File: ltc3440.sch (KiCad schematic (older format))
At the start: 13 parts, among them U1 LTC3440EDD

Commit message: fix 1.5 mhz rt val
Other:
- note added: "RT=60.4k, fsw=1MHz\nRT=45.3k, fsw=1.5MHz\n"
- note removed: "RT=60.4k, fsw=1MHz\nRT=40.4k, fsw=1.5MHz\n"
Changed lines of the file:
@@
 Fixed Freq. Mode
 Text Notes 4400 4950 0    50   ~ 0
-RT=60.4k, fsw=1MHz\nRT=40.4k, fsw=1.5MHz\n
+RT=60.4k, fsw=1MHz\nRT=45.3k, fsw=1.5MHz\n
 $Comp
 L Device:R_Small RT1

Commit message: adds L1 val
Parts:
- L1: value L_Small -> 4.7uH
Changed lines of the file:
@@
 $EndDescr
-$Comp
-L ltc3440:LTC3440EDD U1
-U 1 1 5F6AED89
-P 5600 3600
-F 0 "U1" H 5150 4050 50  0000 C CNN
-F 1 "LTC3440EDD" H 6000 3050 50  0000 C CNN
-F 2 "Package_DFN_QFN:DFN-10-1EP_3x3mm_P0.5mm_EP1.65x2.38mm" H 5750 3050 50  0001 L CNN
-F 3 "https://www.analog.com/media/en/technical-documentation/data-sheets/3440fd.pdf" H 5600 3550 50  0001 C CNN
-F 4 "LTC3440EDD#TRPBFCT-ND" H 5600 3600 50  0001 C CNN "Digikey_PN"
-F 5 "LTC3440EDD#TRPBF" H 5600 3600 50  0001 C CNN "MPN"
-	1    5600 3600
-	1    0    0    -1
-$EndComp
-$Comp
-L Device:L_Small L1
-U 1 1 5F6B38BC
-P 5600 2950
-F 0 "L1" V 5785 2950 50  0000 C CNN
-F 1 "L_Small" V 5694 2950 50  0000 C CNN
-F 2 "" H 5600 2950 50  0001 C CNN
-F 3 "~" H 5600 2950 50  0001 C CNN
-F 4 "CDR43-4R7M" V 5600 2950 50  0001 C CNN "MPN"
-F 5 "SUMIDA " V 5600 2950 50  0001 C CNN "Manufacturer"
-	1    5600 2950
-	0    -1   -1   0
-$EndComp
 $Comp
 L Device:R_Small R1
@@
 $EndComp
 $Comp
-L Device:R_Small R5
-U 1 1 5F6BE50F
-P 7050 3400
-F 0 "R5" H 7109 3446 50  0000 L CNN
-F 1 "10k" H 7109 3355 50  0000 L CNN
-F 2 "" H 7050 3400 50  0001 C CNN
-F 3 "~" H 7050 3400 50  0001 C CNN
-	1    7050 3400
-	1    0    0    -1
-$EndComp
-$Comp
 L power:+3.3V #PWR03
 U 1 1 5F6C1CB3
@@
 Connection ~ 4450 2950
 Wire Wire Line
-	6100 3700 6150 3700
-Wire Wire Line
 	6400 3700 6500 3700
 Wire Wire Line
 	6700 3700 6800 3700
-Wire Wire Line
-	6800 3700 6800 3950
 Wire Wire Line
 	6800 3700 6800 3600
 Connection ~ 6800 3700
 Wire Wire Line
-	6150 3700 6150 3950
-Wire Wire Line
-	6150 3950 6350 3950
-Connection ~ 6150 3700
-Wire Wire Line
-	6150 3700 6200 3700
-Wire Wire Line
-	6550 3950 6800 3950
-Connection ~ 6800 3950
-Wire Wire Line
-	6800 3950 6800 4000
-Wire Wire Line
 	6800 4200 6800 4300
 Wire Wire Line
 	6800 4300 5700 4300
 Connection ~ 5700 4300
-Wire Wire Line
-	7050 3500 7050 3600
-Wire Wire Line
-	7050 3600 6800 3600
 Connection ~ 6800 3600
 Wire Wire Line
 	6800 3600 6800 3500
 Wire Wire Line
-	7050 3600 7350 3600
-Wire Wire Line
 	7350 3600 7350 3700
-Connection ~ 7050 3600
 Wire Wire Line
 	7350 3900 7350 4300
@@
 Connection ~ 6800 4300
 Wire Wire Line
-	7050 3250 7050 3300
-Wire Wire Line
 	7050 2800 7050 3000
 Wire Wire Line
@@
 Connection ~ 7050 3000
 Wire Wire Line
-	7050 3000 7050 3050
-Wire Wire Line
 	7050 3000 7350 3000
 Wire Wire Line
 	7350 3000 7350 3600
 Connection ~ 7350 3600
-$Comp
-L Device:C_Small C5
-U 1 1 5F6BD824
-P 6450 3950
-F 0 "C5" V 6350 4050 50  0000 C CNN
-F 1 "10pF" V 6350 3850 50  0000 C CNN
-F 2 "" H 6450 3950 50  0001 C CNN
-F 3 "~" H 6450 3950 50  0001 C CNN
-	1    6450 3950
-	0    -1   -1   0
-$EndComp
 Connection ~ 6800 3500
 Wire Wire Line
@@
 Wire Wire Line
 	6100 3500 6800 3500
-$Comp
-L Device:C_Small C3
-U 1 1 5F6BDEFF
-P 7050 3150
-F 0 "C3" H 7125 3200 50  0000 L CNN
-F 1 "33pF" H 7100 3075 50  0000 L CNN
-F 2 "" H 7050 3150 50  0001 C CNN
-F 3 "~" H 7050 3150 50  0001 C CNN
-	1    7050 3150
-	1    0    0    -1
-$EndComp
 $Comp
 L Device:D_Schottky_Small_ALT D1
@@
 Wire Wire Line
 	4900 4300 5500 4300
-Text Notes 4400 4750 0    50   ~ 0
-Switching frequency,fsw\nRT = (8*10e10)/fsw\n
 Wire Wire Line
 	4450 2950 4450 3600
@@
 Text Notes 4450 4400 0    50   ~ 0
 Fixed Freq. Mode
-Text Notes 4400 4950 0    50   ~ 0
-RT=60.4k, fsw=1MHz\nRT=45.3k, fsw=1.5MHz\n
 $Comp
 L Device:R_Small RT1
@@
 	1    0    0    -1
 $EndComp
+$Comp
+L ltc3440:LTC3440EDD U1
+U 1 1 5F6AED89
+P 5600 3600
+F 0 "U1" H 5150 4050 50  0000 C CNN
+F 1 "LTC3440EDD" H 6000 3050 50  0000 C CNN
+F 2 "Package_DFN_QFN:DFN-10-1EP_3x3mm_P0.5mm_EP1.65x2.38mm" H 5750 3050 50  0001 L CNN
+F 3 "https://www.analog.com/media/en/technical-documentation/data-sheets/3440fd.pdf" H 5600 3550 50  0001 C CNN
+F 4 "LTC3440EDD#TRPBFCT-ND" H 5600 3600 50  0001 C CNN "Digikey_PN"
+F 5 "LTC3440EDD#TRPBF" H 5600 3600 50  0001 C CNN "MPN"
+	1    5600 3600
+	1    0    0    -1
+$EndComp
+$Comp
+L Device:L_Small L1
+U 1 1 5F6B38BC
+P 5600 2950
+F 0 "L1" V 5785 2950 50  0000 C CNN
+F 1 "4.7uH" V 5694 2950 50  0000 C CNN
+F 2 "" H 5600 2950 50  0001 C CNN
+F 3 "~" H 5600 2950 50  0001 C CNN
+F 4 "CDR43-4R7M" V 5600 2950 50  0001 C CNN "MPN"
+F 5 "SUMIDA " V 5600 2950 50  0001 C CNN "Manufacturer"
+	1    5600 2950
+	0    -1   -1   0
+$EndComp
+Wire Wire Line
+	6150 3700 6200 3700
+Wire Wire Line
+	6100 3700 6150 3700
+Connection ~ 6150 3700
+Wire Wire Line
+	6150 3700 6150 3950
+Wire Wire Line
+	6150 3950 6350 3950
+Wire Wire Line
+	6800 3950 6800 4000
+Wire Wire Line
+	6800 3700 6800 3950
+Connection ~ 6800 3950
+Wire Wire Line
+	6550 3950 6800 3950
+$Comp
+L Device:C_Small C5
+U 1 1 5F6BD824
+P 6450 3950
+F 0 "C5" V 6350 4050 50  0000 C CNN
+F 1 "10pF" V 6350 3850 50  0000 C CNN
+F 2 "" H 6450 3950 50  0001 C CNN
+F 3 "~" H 6450 3950 50  0001 C CNN
+	1    6450 3950
+	0    -1   -1   0
+$EndComp
+Wire Wire Line
+	7050 3000 7050 3050
+Wire Wire Line
+	7050 3600 7350 3600
+Wire Wire Line
+	7050 3600 6800 3600
+Connection ~ 7050 3600
+Wire Wire Line
+	7050 3500 7050 3600
+Wire Wire Line
+	7050 3250 7050 3300
+$Comp
+L Device:C_Small C3
+U 1 1 5F6BDEFF
+P 7050 3150
+F 0 "C3" H 7125 3200 50  0000 L CNN
+F 1 "33pF" H 7100 3075 50  0000 L CNN
+F 2 "" H 7050 3150 50  0001 C CNN
+F 3 "~" H 7050 3150 50  0001 C CNN
+	1    7050 3150
+	1    0    0    -1
+$EndComp
+$Comp
+L Device:R_Small R5
+U 1 1 5F6BE50F
+P 7050 3400
+F 0 "R5" H 7109 3446 50  0000 L CNN
+F 1 "10k" H 7109 3355 50  0000 L CNN
+F 2 "" H 7050 3400 50  0001 C CNN
+F 3 "~" H 7050 3400 50  0001 C CNN
+	1    7050 3400
+	1    0    0    -1
+$EndComp
+Text Notes 4400 4750 0    50   ~ 0
+Switching frequency,fsw\nRT = (8*10e10)/fsw\n
 Text Notes 4650 4250 0    50   ~ 0
 1%
+Text Notes 4400 4950 0    50   ~ 0
+RT=60.4k, fsw=1MHz\nRT=45.3k, fsw=1.5MHz\n
 $EndSCHEMATC

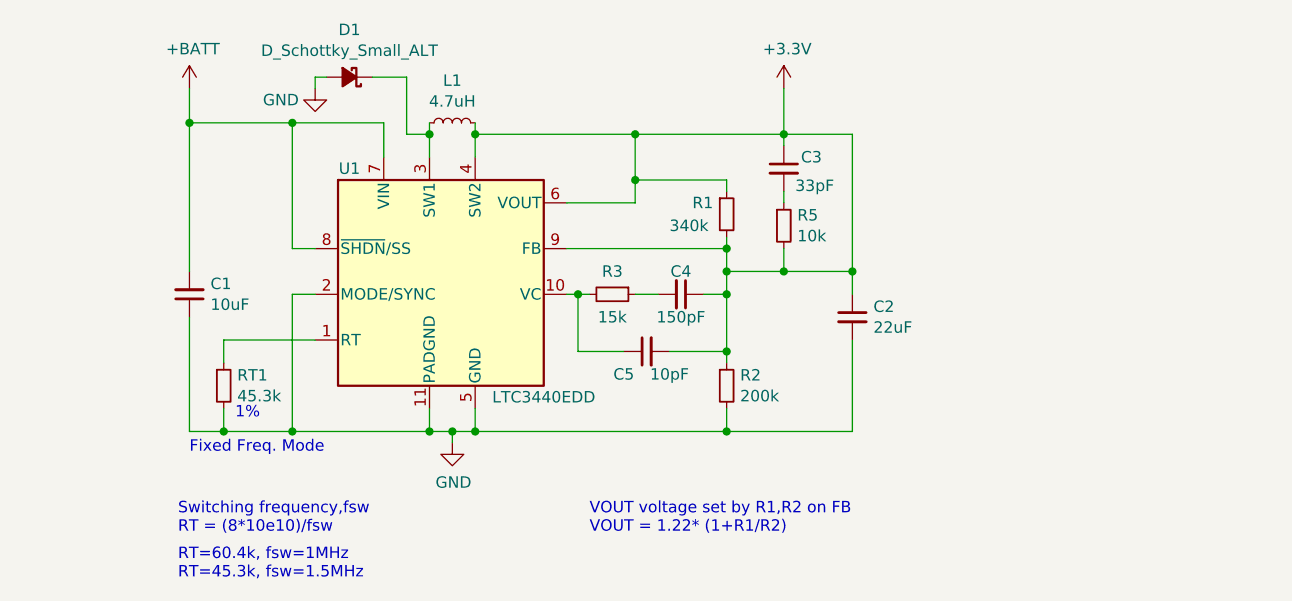
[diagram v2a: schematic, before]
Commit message: update to follow application from datasheet page1
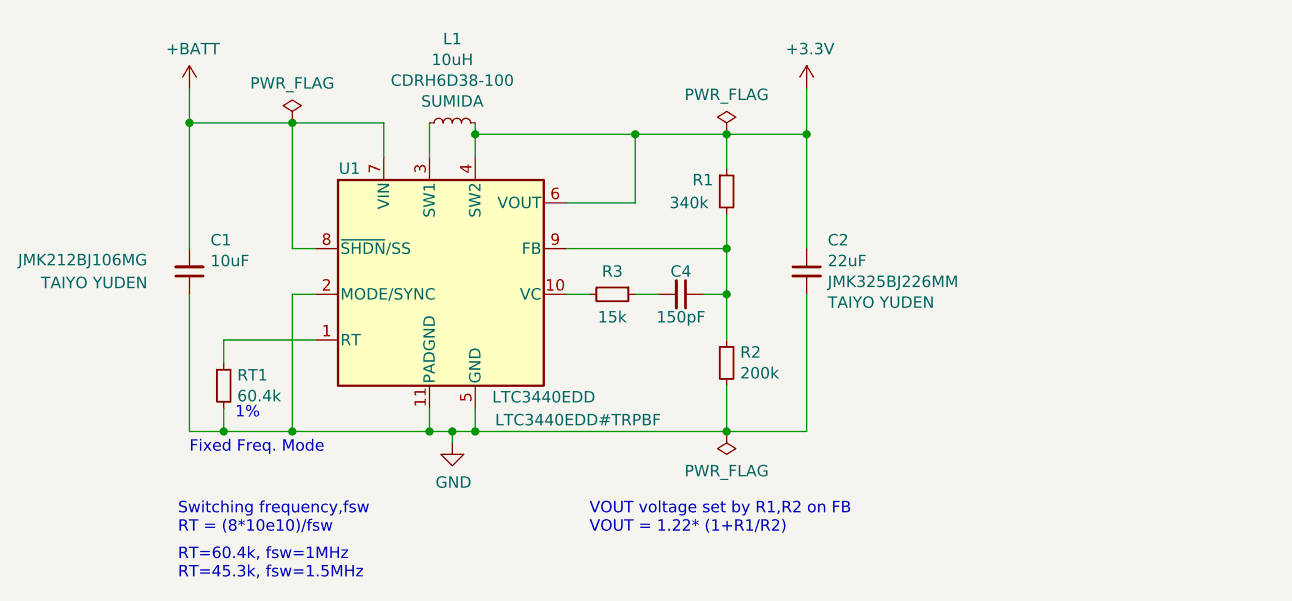
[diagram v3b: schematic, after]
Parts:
- removed C3: 33pF, symbol Device:C_Small
- removed C5: 10pF, symbol Device:C_Small
- removed D1: D_Schottky_Small_ALT, symbol Device:D_Schottky_Small_ALT
- removed R5: 10k, symbol Device:R_Small
- C1, C2: footprint (none) -> Capacitor_SMD:C_1206_3216Metric
- L1: value 4.7uH -> 10uH; Digikey_PN (none) -> 308-1541-2-ND; MPN CDR43-4R7M -> CDRH6D38-100
- RT1: value 45.3k -> 60.4k
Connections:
- net +3V3: no longer C4.1, R1.2, R2.1, U1.9 (FB)
- new net: C4.1, R1.2, R2.1, U1.9 (FB)
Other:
- moved on the sheet: C1, C2, R1, R2
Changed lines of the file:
@@
 L Device:R_Small R1
 U 1 1 5F6B5492
-P 6800 3350
-F 0 "R1" H 6650 3400 50  0000 L CNN
-F 1 "340k" H 6550 3300 50  0000 L CNN
-F 2 "" H 6800 3350 50  0001 C CNN
-F 3 "~" H 6800 3350 50  0001 C CNN
-	1    6800 3350
+P 6800 3250
+F 0 "R1" H 6650 3300 50  0000 L CNN
+F 1 "340k" H 6550 3200 50  0000 L CNN
+F 2 "" H 6800 3250 50  0001 C CNN
+F 3 "~" H 6800 3250 50  0001 C CNN
+	1    6800 3250
 	1    0    0    -1
 $EndComp
@@
 L Device:R_Small R2
 U 1 1 5F6B5CEC
-P 6800 4100
-F 0 "R2" H 6859 4146 50  0000 L CNN
-F 1 "200k" H 6859 4055 50  0000 L CNN
-F 2 "" H 6800 4100 50  0001 C CNN
-F 3 "~" H 6800 4100 50  0001 C CNN
-	1    6800 4100
+P 6800 4000
+F 0 "R2" H 6859 4046 50  0000 L CNN
+F 1 "200k" H 6859 3955 50  0000 L CNN
+F 2 "" H 6800 4000 50  0001 C CNN
+F 3 "~" H 6800 4000 50  0001 C CNN
+	1    6800 4000
 	1    0    0    -1
 $EndComp
@@
 L Device:C_Small C2
 U 1 1 5F6B6FD3
-P 7350 3800
-F 0 "C2" H 7442 3846 50  0000 L CNN
-F 1 "22uF" H 7442 3755 50  0000 L CNN
-F 2 "" H 7350 3800 50  0001 C CNN
-F 3 "~" H 7350 3800 50  0001 C CNN
-F 4 "JMK325BJ226MM" H 7350 3800 50  0001 C CNN "MPN"
-F 5 "TAIYO YUDEN" H 7350 3800 50  0001 C CNN "Manufacturer"
-	1    7350 3800
+P 7150 3600
+F 0 "C2" H 7242 3737 50  0000 L CNN
+F 1 "22uF" H 7242 3646 50  0000 L CNN
+F 2 "Capacitor_SMD:C_1206_3216Metric" H 7150 3600 50  0001 C CNN
+F 3 "~" H 7150 3600 50  0001 C CNN
+F 4 "JMK325BJ226MM" H 7242 3555 50  0000 L CNN "MPN"
+F 5 "TAIYO YUDEN" H 7242 3464 50  0000 L CNN "Manufacturer"
+	1    7150 3600
 	1    0    0    -1
 $EndComp
@@
 L Device:C_Small C1
 U 1 1 5F6B880E
-P 4450 3700
-F 0 "C1" H 4358 3654 50  0000 R CNN
-F 1 "10uF" H 4358 3745 50  0000 R CNN
-F 2 "" H 4450 3700 50  0001 C CNN
-F 3 "~" H 4450 3700 50  0001 C CNN
-F 4 "JMK212BJ106MG" H 4450 3700 50  0001 C CNN "MPN"
-F 5 "TAIYO YUDEN" H 4450 3700 50  0001 C CNN "Manufacturer"
-	1    4450 3700
+P 4450 3600
+F 0 "C1" H 4358 3463 50  0000 R CNN
+F 1 "10uF" H 4358 3554 50  0000 R CNN
+F 2 "Capacitor_SMD:C_1206_3216Metric" H 4450 3600 50  0001 C CNN
+F 3 "~" H 4450 3600 50  0001 C CNN
+F 4 "JMK212BJ106MG" H 5200 3550 50  0000 R CNN "MPN"
+F 5 "TAIYO YUDEN" H 5100 3650 50  0000 R CNN "Manufacturer"
+	1    4450 3600
 	-1   0    0    1
 $EndComp
@@
 L power:+3.3V #PWR03
 U 1 1 5F6C1CB3
-P 7050 2800
-F 0 "#PWR03" H 7050 2650 50  0001 C CNN
-F 1 "+3.3V" H 7065 2973 50  0000 C CNN
-F 2 "" H 7050 2800 50  0001 C CNN
-F 3 "" H 7050 2800 50  0001 C CNN
-	1    7050 2800
+P 7150 2800
+F 0 "#PWR03" H 7150 2650 50  0001 C CNN
+F 1 "+3.3V" H 7165 2973 50  0000 C CNN
+F 2 "" H 7150 2800 50  0001 C CNN
+F 3 "" H 7150 2800 50  0001 C CNN
+	1    7150 2800
 	1    0    0    -1
 $EndComp
@@
 	4600 3900 5000 3900
 Wire Wire Line
-	4450 3800 4450 4300
+	4450 3700 4450 4300
 Wire Wire Line
 	4450 4300 4600 4300
@@
 Wire Wire Line
 	6700 3700 6800 3700
-Wire Wire Line
-	6800 3700 6800 3600
 Connection ~ 6800 3700
 Wire Wire Line
-	6800 4200 6800 4300
+	6800 4100 6800 4300
 Wire Wire Line
 	6800 4300 5700 4300
 Connection ~ 5700 4300
-Connection ~ 6800 3600
-Wire Wire Line
-	6800 3600 6800 3500
-Wire Wire Line
-	7350 3600 7350 3700
-Wire Wire Line
-	7350 3900 7350 4300
-Wire Wire Line
-	7350 4300 6800 4300
+Wire Wire Line
+	7150 3700 7150 4300
+Wire Wire Line
+	7150 4300 6800 4300
 Connection ~ 6800 4300
 Wire Wire Line
-	7050 2800 7050 3000
+	7150 2800 7150 3000
 Wire Wire Line
 	6100 3300 6400 3300
-Wire Wire Line
-	6400 3300 6400 3200
-Wire Wire Line
-	6400 3200 6800 3200
-Wire Wire Line
-	6800 3200 6800 3250
-Connection ~ 6400 3200
-Wire Wire Line
-	6400 3200 6400 3000
 Wire Wire Line
 	6400 3000 5700 3000
@@
 	5700 3000 5700 3100
 Wire Wire Line
-	5500 2950 5500 3000
-Wire Wire Line
-	6400 3000 7050 3000
-Connection ~ 7050 3000
-Wire Wire Line
-	7050 3000 7350 3000
-Wire Wire Line
-	7350 3000 7350 3600
-Connection ~ 7350 3600
+	6400 3000 6800 3000
+Connection ~ 7150 3000
 Connection ~ 6800 3500
 Wire Wire Line
-	6800 3500 6800 3450
+	6800 3500 6800 3350
 Wire Wire Line
 	6100 3500 6800 3500
-$Comp
-L Device:D_Schottky_Small_ALT D1
-U 1 1 5F70336F
-P 5150 2750
-F 0 "D1" H 5150 2543 50  0000 C CNN
-F 1 "D_Schottky_Small_ALT" H 5150 2634 50  0000 C CNN
-F 2 "" V 5150 2750 50  0001 C CNN
-F 3 "~" V 5150 2750 50  0001 C CNN
-F 4 "CMDSH2-3" H 5150 2750 50  0001 C CNN "MPN"
-F 5 "CENTRAL SEMICONDUCTOR " H 5150 2750 50  0001 C CNN "Manufacturer"
-	1    5150 2750
-	-1   0    0    1
-$EndComp
-$Comp
-L power:GND #PWR02
-U 1 1 5F703CEF
-P 5000 2800
-F 0 "#PWR02" H 5000 2550 50  0001 C CNN
-F 1 "GND" H 4850 2750 50  0000 C CNN
-F 2 "" H 5000 2800 50  0001 C CNN
-F 3 "" H 5000 2800 50  0001 C CNN
-	1    5000 2800
-	1    0    0    -1
-$EndComp
-Wire Wire Line
-	5050 2750 5000 2750
-Wire Wire Line
-	5000 2750 5000 2800
-Wire Wire Line
-	5250 2750 5400 2750
-Wire Wire Line
-	5400 2750 5400 3000
-Wire Wire Line
-	5400 3000 5500 3000
-Connection ~ 5500 3000
-Wire Wire Line
-	5500 3000 5500 3100
 Wire Wire Line
 	5000 3700 4900 3700
@@
 	4900 4300 5500 4300
 Wire Wire Line
-	4450 2950 4450 3600
+	4450 2950 4450 3500
 Wire Wire Line
 	5000 3500 4900 3500
@@
 VOUT voltage set by R1,R2 on FB\nVOUT = 1.22* (1+R1/R2)
 Connection ~ 6400 3000
-Text Notes 4450 4400 0    50   ~ 0
-Fixed Freq. Mode
 $Comp
 L Device:R_Small RT1
@@
 P 4600 4100
 F 0 "RT1" H 4659 4146 50  0000 L CNN
-F 1 "45.3k" H 4659 4055 50  0000 L CNN
+F 1 "60.4k" H 4659 4055 50  0000 L CNN
 F 2 "" H 4600 4100 50  0001 C CNN
 F 3 "~" H 4600 4100 50  0001 C CNN
@@
 F 2 "Package_DFN_QFN:DFN-10-1EP_3x3mm_P0.5mm_EP1.65x2.38mm" H 5750 3050 50  0001 L CNN
 F 3 "https://www.analog.com/media/en/technical-documentation/data-sheets/3440fd.pdf" H 5600 3550 50  0001 C CNN
-F 4 "LTC3440EDD#TRPBFCT-ND" H 5600 3600 50  0001 C CNN "Digikey_PN"
-F 5 "LTC3440EDD#TRPBF" H 5600 3600 50  0001 C CNN "MPN"
+F 4 "LTC3440EDD#TRPBFCT-ND" H 6250 2950 50  0001 C CNN "Digikey_PN"
+F 5 "LTC3440EDD#TRPBF" H 6150 2950 50  0000 C CNN "MPN"
 	1    5600 3600
 	1    0    0    -1
@@
 U 1 1 5F6B38BC
 P 5600 2950
-F 0 "L1" V 5785 2950 50  0000 C CNN
-F 1 "4.7uH" V 5694 2950 50  0000 C CNN
+F 0 "L1" V 5967 2950 50  0000 C CNN
+F 1 "10uH" V 5876 2950 50  0000 C CNN
 F 2 "" H 5600 2950 50  0001 C CNN
 F 3 "~" H 5600 2950 50  0001 C CNN
-F 4 "CDR43-4R7M" V 5600 2950 50  0001 C CNN "MPN"
-F 5 "SUMIDA " V 5600 2950 50  0001 C CNN "Manufacturer"
+F 4 "CDRH6D38-100" V 5785 2950 50  0000 C CNN "MPN"
+F 5 "SUMIDA " V 5694 2950 50  0000 C CNN "Manufacturer"
+F 6 "308-1541-2-ND" V 5600 2950 50  0001 C CNN "Digikey_PN"
 	1    5600 2950
 	0    -1   -1   0
-$EndComp
-Wire Wire Line
-	6150 3700 6200 3700
-Wire Wire Line
-	6100 3700 6150 3700
-Connection ~ 6150 3700
-Wire Wire Line
-	6150 3700 6150 3950
-Wire Wire Line
-	6150 3950 6350 3950
-Wire Wire Line
-	6800 3950 6800 4000
-Wire Wire Line
-	6800 3700 6800 3950
-Connection ~ 6800 3950
-Wire Wire Line
-	6550 3950 6800 3950
-$Comp
-L Device:C_Small C5
-U 1 1 5F6BD824
-P 6450 3950
-F 0 "C5" V 6350 4050 50  0000 C CNN
-F 1 "10pF" V 6350 3850 50  0000 C CNN
-F 2 "" H 6450 3950 50  0001 C CNN
-F 3 "~" H 6450 3950 50  0001 C CNN
-	1    6450 3950
-	0    -1   -1   0
-$EndComp
-Wire Wire Line
-	7050 3000 7050 3050
-Wire Wire Line
-	7050 3600 7350 3600
-Wire Wire Line
-	7050 3600 6800 3600
-Connection ~ 7050 3600
-Wire Wire Line
-	7050 3500 7050 3600
-Wire Wire Line
-	7050 3250 7050 3300
-$Comp
-L Device:C_Small C3
-U 1 1 5F6BDEFF
-P 7050 3150
-F 0 "C3" H 7125 3200 50  0000 L CNN
-F 1 "33pF" H 7100 3075 50  0000 L CNN
-F 2 "" H 7050 3150 50  0001 C CNN
-F 3 "~" H 7050 3150 50  0001 C CNN
-	1    7050 3150
-	1    0    0    -1
-$EndComp
-$Comp
-L Device:R_Small R5
-U 1 1 5F6BE50F
-P 7050 3400
-F 0 "R5" H 7109 3446 50  0000 L CNN
-F 1 "10k" H 7109 3355 50  0000 L CNN
-F 2 "" H 7050 3400 50  0001 C CNN
-F 3 "~" H 7050 3400 50  0001 C CNN
-	1    7050 3400
-	1    0    0    -1
 $EndComp
 Text Notes 4400 4750 0    50   ~ 0
@@
 Text Notes 4400 4950 0    50   ~ 0
 RT=60.4k, fsw=1MHz\nRT=45.3k, fsw=1.5MHz\n
+Wire Wire Line
+	6800 3700 6800 3900
+Wire Wire Line
+	6100 3700 6200 3700
+Wire Wire Line
+	5500 2950 5500 3100
+Wire Wire Line
+	6800 3500 6800 3700
+Wire Wire Line
+	7150 3000 7150 3500
+Wire Wire Line
+	6400 3000 6400 3300
+Wire Wire Line
+	6800 3000 6800 3150
+Connection ~ 6800 3000
+Wire Wire Line
+	6800 3000 7150 3000
+Text Notes 4450 4400 0    50   ~ 0
+Fixed Freq. Mode
+$Comp
+L power:PWR_FLAG #FLG?
+U 1 1 5F742A39
+P 4900 2950
+F 0 "#FLG?" H 4900 3025 50  0001 C CNN
+F 1 "PWR_FLAG" H 4900 3123 50  0000 C CNN
+F 2 "" H 4900 2950 50  0001 C CNN
+F 3 "~" H 4900 2950 50  0001 C CNN
+	1    4900 2950
+	1    0    0    -1
+$EndComp
+$Comp
+L power:PWR_FLAG #FLG?
+U 1 1 5F743DCE
+P 6800 3000
+F 0 "#FLG?" H 6800 3075 50  0001 C CNN
+F 1 "PWR_FLAG" H 6800 3173 50  0000 C CNN
+F 2 "" H 6800 3000 50  0001 C CNN
+F 3 "~" H 6800 3000 50  0001 C CNN
+	1    6800 3000
+	1    0    0    -1
+$EndComp
+$Comp
+L power:PWR_FLAG #FLG?
+U 1 1 5F74412F
+P 6800 4300
+F 0 "#FLG?" H 6800 4375 50  0001 C CNN
+F 1 "PWR_FLAG" H 6800 4473 50  0000 C CNN
+F 2 "" H 6800 4300 50  0001 C CNN
+F 3 "~" H 6800 4300 50  0001 C CNN
+	1    6800 4300
+	-1   0    0    1
+$EndComp
 $EndSCHEMATC

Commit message: adds footprints
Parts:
- C4: footprint (none) -> Capacitor_SMD:C_0603_1608Metric_Pad1.05x0.95mm_HandSolder
- L1: footprint (none) -> ltc3440:L_Sumida-CDRH6D38
- R1, R2, R3, RT1: footprint (none) -> Resistor_SMD:R_0603_1608Metric_Pad1.05x0.95mm_HandSolder
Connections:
- net at R1.2, R2.1, U1.9 (FB): now also C4.2; no longer C4.1
- net at R3.1: now also C4.1; no longer C4.2
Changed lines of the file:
@@
 F 0 "R1" H 6650 3300 50  0000 L CNN
 F 1 "340k" H 6550 3200 50  0000 L CNN
-F 2 "" H 6800 3250 50  0001 C CNN
+F 2 "Resistor_SMD:R_0603_1608Metric_Pad1.05x0.95mm_HandSolder" H 6800 3250 50  0001 C CNN
 F 3 "~" H 6800 3250 50  0001 C CNN
 	1    6800 3250
@@
 F 0 "R2" H 6859 4046 50  0000 L CNN
 F 1 "200k" H 6859 3955 50  0000 L CNN
-F 2 "" H 6800 4000 50  0001 C CNN
+F 2 "Resistor_SMD:R_0603_1608Metric_Pad1.05x0.95mm_HandSolder" H 6800 4000 50  0001 C CNN
 F 3 "~" H 6800 4000 50  0001 C CNN
 	1    6800 4000
@@
 F 0 "R3" V 6200 3700 50  0000 C CNN
 F 1 "15k" V 6400 3700 50  0000 C CNN
-F 2 "" H 6300 3700 50  0001 C CNN
+F 2 "Resistor_SMD:R_0603_1608Metric_Pad1.05x0.95mm_HandSolder" H 6300 3700 50  0001 C CNN
 F 3 "~" H 6300 3700 50  0001 C CNN
 	1    6300 3700
@@
 F 0 "C4" V 6500 3700 50  0000 C CNN
 F 1 "150pF" V 6700 3700 50  0000 C CNN
-F 2 "" H 6600 3700 50  0001 C CNN
+F 2 "Capacitor_SMD:C_0603_1608Metric_Pad1.05x0.95mm_HandSolder" H 6600 3700 50  0001 C CNN
 F 3 "~" H 6600 3700 50  0001 C CNN
 	1    6600 3700
-	0    1    1    0
+	0    -1   -1   0
 $EndComp
 $Comp
@@
 F 0 "RT1" H 4659 4146 50  0000 L CNN
 F 1 "60.4k" H 4659 4055 50  0000 L CNN
-F 2 "" H 4600 4100 50  0001 C CNN
+F 2 "Resistor_SMD:R_0603_1608Metric_Pad1.05x0.95mm_HandSolder" H 4600 4100 50  0001 C CNN
 F 3 "~" H 4600 4100 50  0001 C CNN
 	1    4600 4100
@@
 F 0 "L1" V 5967 2950 50  0000 C CNN
 F 1 "10uH" V 5876 2950 50  0000 C CNN
-F 2 "" H 5600 2950 50  0001 C CNN
+F 2 "ltc3440:L_Sumida-CDRH6D38" H 5600 2950 50  0001 C CNN
 F 3 "~" H 5600 2950 50  0001 C CNN
 F 4 "CDRH6D38-100" V 5785 2950 50  0000 C CNN "MPN"
